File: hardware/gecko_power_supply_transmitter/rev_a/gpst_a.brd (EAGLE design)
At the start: 32.5 x 38.7 mm, 7 parts, among them J1 EPIC-PROG-POGO-NO-LEGS, J2 GECKO_POWER_SUPPLY_CONN, U1 EPIC-CORE_A

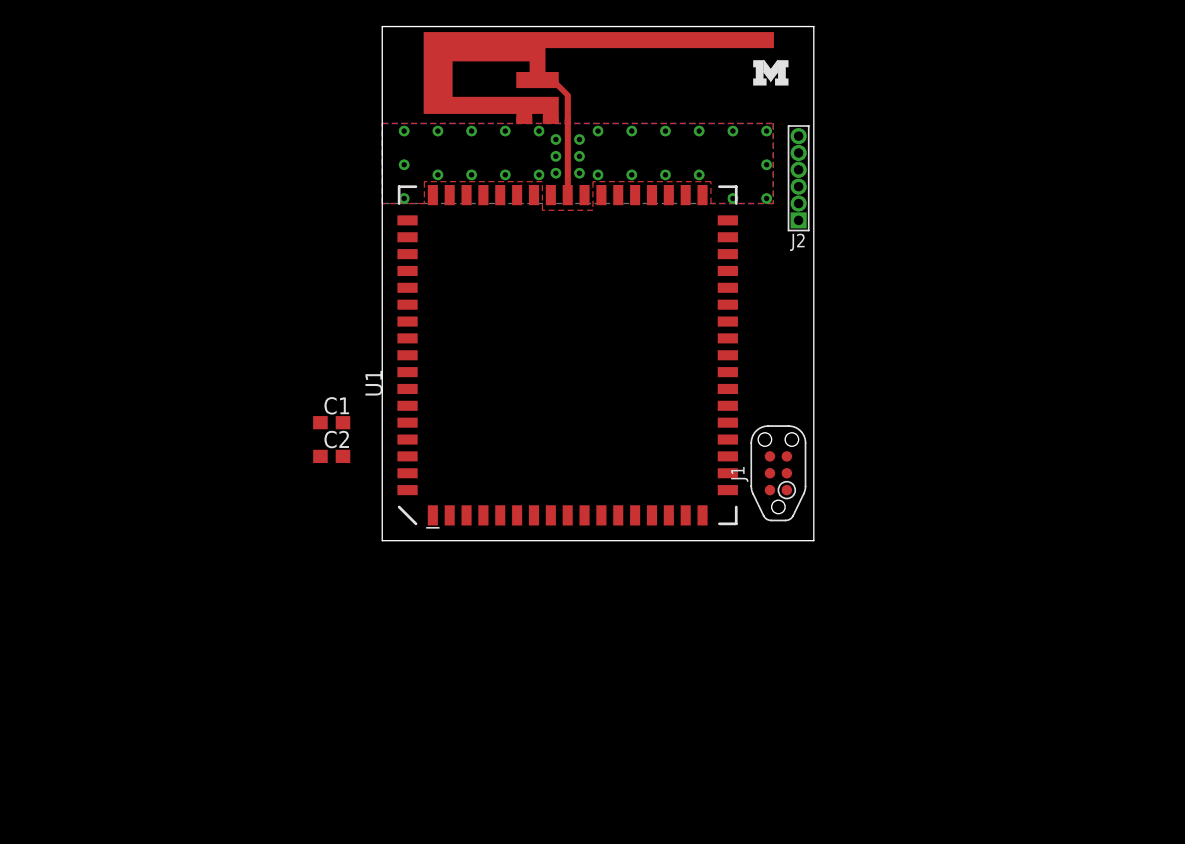
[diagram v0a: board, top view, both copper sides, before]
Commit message: no longer using epic
cc2538 and chip antenna ftw
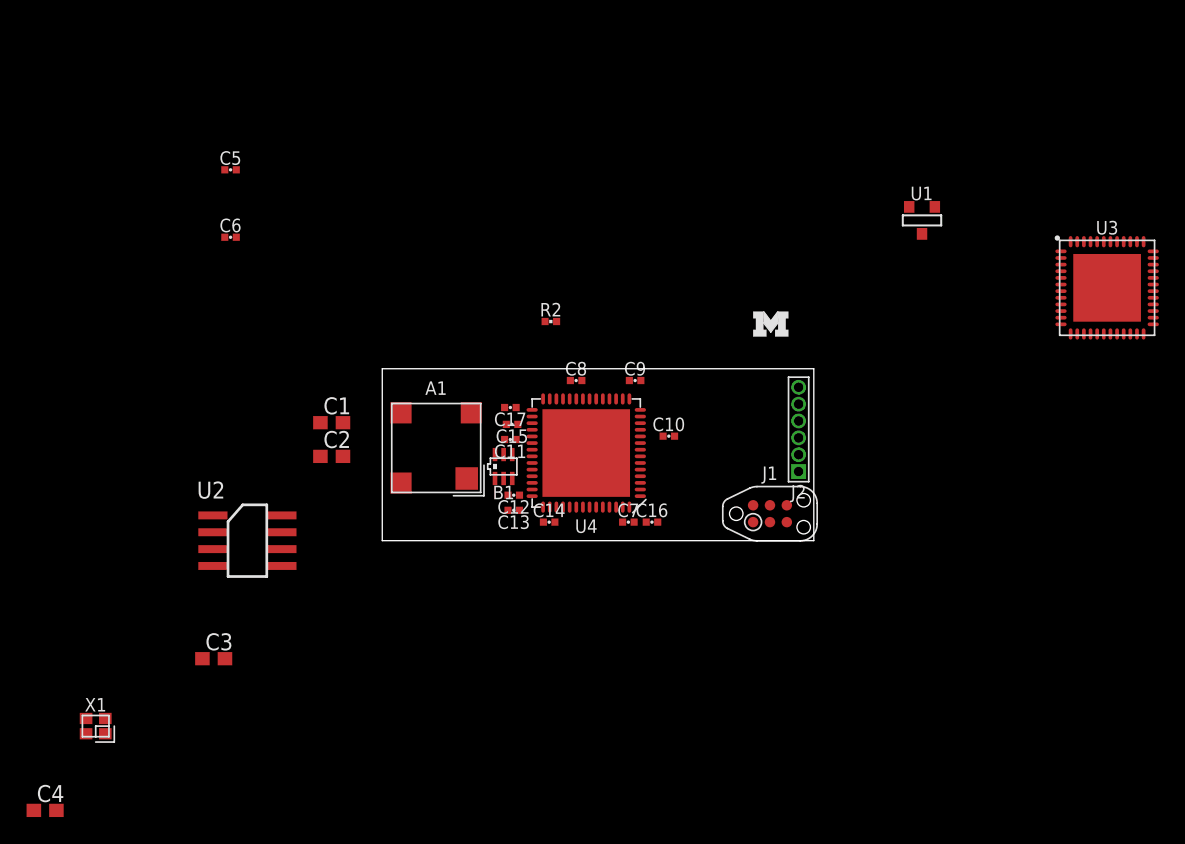
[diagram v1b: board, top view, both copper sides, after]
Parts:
- removed ANT1: PIFA-2.4GHZ, epic:PIFA-2.4GHZ
- added A1: FRACTUS-2.4GHZ-FR05-S1-N-0-001, chips:FRACTUS-ANTENNA-FR05-S1-N-0-001
- added B1: 2450BM15A0002, chips:2450BM
- added C10, C11, C12, C14, C15, C8, C9: 100nF, passives:0402_CAP
- added C13: 220pF, passives:0402_CAP
- added C16, C17, C7: 1uF, passives:0402_CAP
- added C3, C4: 0.1uF, rcl:C0603
- added C5, C6: 12pF, passives:0402_CAP
- added R2: (no value), passives:0402_RES
- added U2: FM25LB, chips:SOIC_8
- added U3: MSP430FR5969, chips:RGZ(S-PQFP-N48)
- added U4: CC2538, chips:S-PVQFN-N56
- added X1: EPSON-FA-128, crystals:FA-128
- U1: value EPIC-CORE_A -> DS2411; device epic:EPIC-LCC68 -> chips:SOT-23
- moved U1 28.5 mm to (40.6, 24.1), turned to 0 degrees
- moved J2 18.9 mm to (31.4, 7.75)
- moved U$1 18.9 mm to (27.9, 15.4)
- moved J1 3.11 mm to (29.2, 2.03), turned to 0 degrees
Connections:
- removed net N$1: ANT1.P$1, U1.P$43
- removed net RFGND: ANT1.P$2, ANT1.P$3, U1.P$42, U1.P$44
- new net N$10: C6.1, U4.35, X1.3
- new net N$15: C16.1, C17.1, U4.32, U4.56
- new net N$5: B1.4, U4.37
- new net N$6: B1.3, U4.38
- new net N$7: A1.1, B1.1
- new net N$9: C5.1, U4.34, X1.1
- net !RST: no longer U1.P$16
- net GND: now also B1.2, B1.5, B1.6, C10.2, C11.2, C12.2, C13.2, C14.2, C15.2, C16.2, C17.2, C3.2, C5.2, C6.2, C7.2, C8.2, C9.2, U2.P4, U4.VSS_QFN, X1.2, X1.4; no longer U1.P$1, U1.P$18, U1.P$35, U1.P$52
- net RX: no longer U1.P$62
- net TCK: no longer U1.P$15
- net TX: no longer U1.P$61
- net VCC: now also C10.1, C11.1, C12.1, C13.1, C14.1, C15.1, C3.1, C7.1, C8.1, C9.1, U2.P8, U4.10, U4.15, U4.24, U4.33, U4.36, U4.39, U4.40, U4.41, U4.43, U4.55; no longer U1.P$17, U1.P$68
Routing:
- net N$1: track 5.61 -> 0.00 mm
- removed copper zone on layer 1, net RFGND
- removed copper zone on layer 16, net RFGND
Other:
- board size 32.5 x 38.7 mm -> 32.5 x 13 mm

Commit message: routed except for vcc
the transmitter board is coming along nicely.
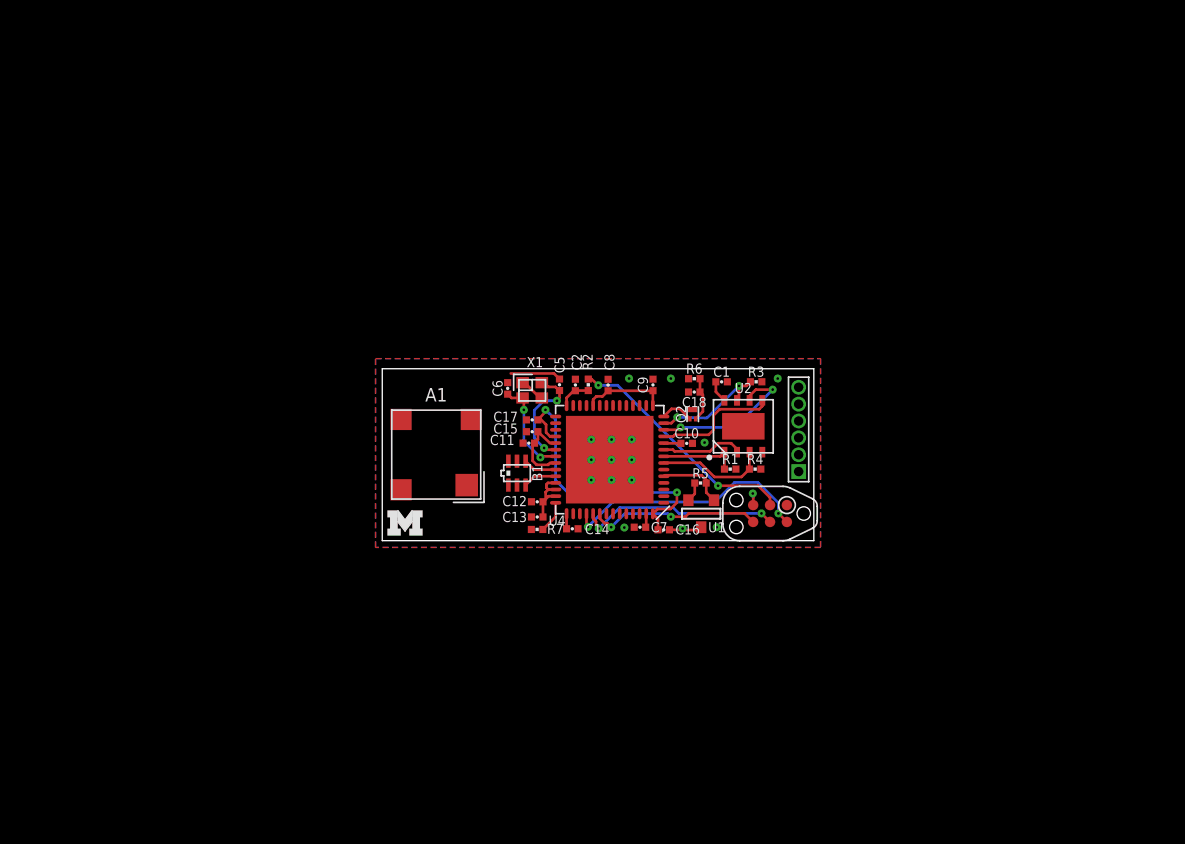
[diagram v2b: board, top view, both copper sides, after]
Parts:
- removed C3, C4: 0.1uF, rcl:C0603
- removed J1: EPIC-PROG-POGO-NO-LEGS, epic:TC2030-IDC-NL
- removed U3: MSP430FR5969, chips:RGZ(S-PQFP-N48)
- added C18: 2.2uF, passives:0402_CAP
- added J3: TC2030-CTX-NL, connector:TC2030-IDC-NL
- added Q2: MOSFET-NCHANNELXFDN-3, fets:XFDFN-3
- added R1, R3, R4: 4.7k, passives:0402_RES
- added R5: 2.2k, passives:0402_RES
- added R6: 4.7M, passives:0402_RES
- added R7: 56k, passives:0402_RES
- C1: device rcl:C0603 -> passives:0402_CAP
- C2: value 0.1uF -> 1nF; device rcl:C0603 -> passives:0402_CAP
- R2: value (none) -> 2.2k
- U2: value FM25LB -> FM25LBTDFN-8; device chips:SOIC_8 -> chips:TDFN-8
- moved X1 41.5 mm to (11.3, 11.3), turned to 180 degrees
- moved U2 38.3 mm to (27.2, 8.62)
- moved U$1 31.4 mm to (0.38, 0.38)
- moved C5 29.6 mm to (13.4, 11.7), turned to 90 degrees
- moved C1 29.5 mm to (25.6, 12.0)
- moved U1 27.7 mm to (24.0, 2.03)
- moved C6 23.8 mm to (9.45, 11.5), turned to 90 degrees
- moved C2 19.1 mm to (14.6, 11.7), turned to 90 degrees
- moved R2 5.54 mm to (15.5, 11.7), turned to 270 degrees
- moved C8 2.43 mm to (17.0, 11.7), turned to 90 degrees
- moved C17 1.89 mm to (11.3, 9.10)
- moved C12 1.84 mm to (11.7, 2.93)
- moved C13 1.84 mm to (11.7, 1.79)
- moved U4 1.84 mm to (17.1, 6.10)
- moved C14 1.81 mm to (14.3, 0.90)
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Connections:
- removed net !RST: J1.6
- removed net RX: J1.4
- removed net TX: J1.3
- new net !FRAM_CS: R1.1, U2.1, U4.8
- new net !FRAM_HOLD: R3.1, U2.7, U4.13
- new net !FRAM_WP: R4.1, U2.3, U4.7
- new net !RESET: J3.3, R2.1
- new net DS2411: R5.1, U1.1, U4.5
- new net MISO: U2.2, U4.9
- new net MOSI: U2.5, U4.11
- new net N$1: C2.1, R2.2, U4.28
- new net N$11: C18.1, Q2.S, R6.2
- new net SCK: U2.6, U4.12
- new net TDI: U4.49
- new net TDO: J3.6, U4.48
- new net TIME_CTL: Q2.G, U4.14
- new net TMS: J3.2, U4.46
- net GND: now also C18.2, C2.2, J3.5, R6.1, R7.2, U1.3, U2.4; no longer C3.2, J1.2, U2.P4
- net N$8: now also R7.1, U4.42; no longer C2.2
- net TCK: now also J3.4, U4.47; no longer J1.5
- net VCC: now also J3.1, Q2.D, R1.2, R3.2, R4.2, R5.2, U1.2, U2.8; no longer C2.1, C3.1, J1.1, U2.P8
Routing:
- net VCC: track 0.00 -> 24.0 mm
- net N$15: track 0.00 -> 22.7 mm, vias 0 -> 2
- net TMS: track 0.00 -> 19.1 mm, vias 0 -> 2
- net !RESET: track 0.00 -> 17.9 mm, vias 0 -> 2
- net TCK: track 0.00 -> 15.3 mm, vias 0 -> 2
- net TDO: track 0.00 -> 13.6 mm, vias 0 -> 2
- net SCK: track 0.00 -> 12.0 mm, vias 0 -> 2
- net MOSI: track 0.00 -> 9.43 mm
- net GND: track 0.00 -> 9.13 mm, vias 0 -> 17
- net !FRAM_HOLD: track 0.00 -> 8.99 mm, vias 0 -> 2
- net N$9: track 0.00 -> 8.45 mm, vias 0 -> 2
- net !FRAM_WP: track 0.00 -> 8.42 mm
- net N$10: track 0.00 -> 7.46 mm, vias 0 -> 2
- net MISO: track 0.00 -> 6.24 mm
- net !FRAM_CS: track 0.00 -> 5.97 mm
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- added copper zone on layer 1, net GND
- added copper zone on layer 16, net GND

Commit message: getting closer with vcc
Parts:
- moved B1 0.51 mm to (9.64, 5.09)
- moved C15 0.46 mm to (11.0, 8.59)
- moved C11 0.43 mm to (11.0, 7.78)
- moved C17 0.42 mm to (11.0, 9.43)
- moved C10 0.33 mm to (23.3, 7.33)
- moved R5 0.20 mm to (24.0, 4.14)
- moved R1 0.18 mm to (26.3, 5.57)
- moved C18 0.10 mm to (23.5, 11.3)
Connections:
- removed net N$11: C18.1, Q2.S, R6.2
- new net V_TIMER: C18.1, Q2.S, R6.2, U4.16
- net SHD: now also U4.6
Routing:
- net VCC: track 24.0 -> 62.7 mm, vias 0 -> 9
- net SHD: track 0.00 -> 12.2 mm, vias 0 -> 1
- net V_TIMER: track 0.00 -> 9.22 mm, vias 0 -> 2
- net GND: track 9.13 -> 13.1 mm, vias 17 -> 21
- net N$11: track 3.34 -> 0.00 mm
- net N$10: track 7.46 -> 8.72 mm
- net !RESET: track 17.9 -> 19.1 mm
- net N$6: track 2.54 -> 3.04 mm
- net N$5: track 2.52 -> 3.03 mm

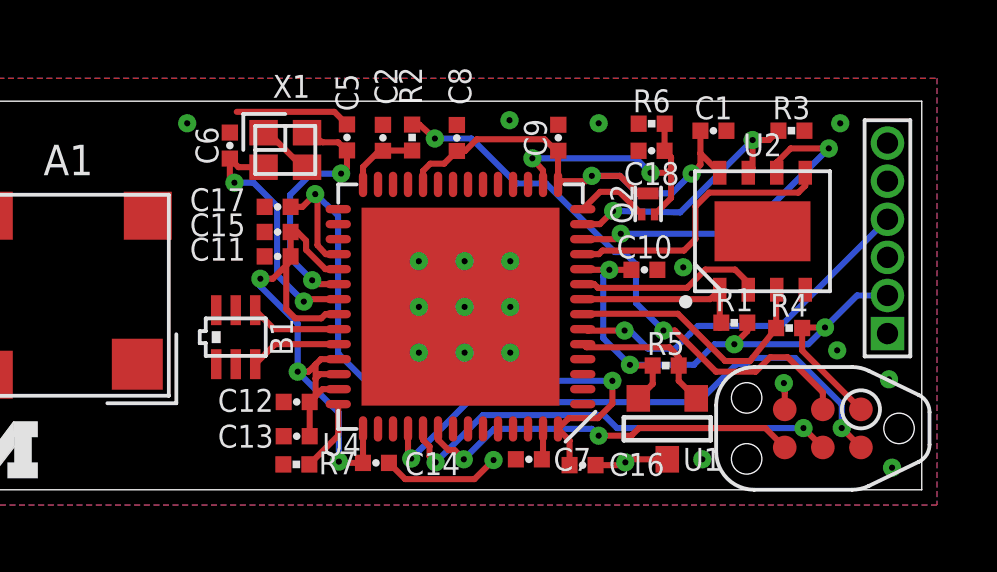
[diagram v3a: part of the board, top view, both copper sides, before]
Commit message: routed except antenna
now 4 layers cause its easier
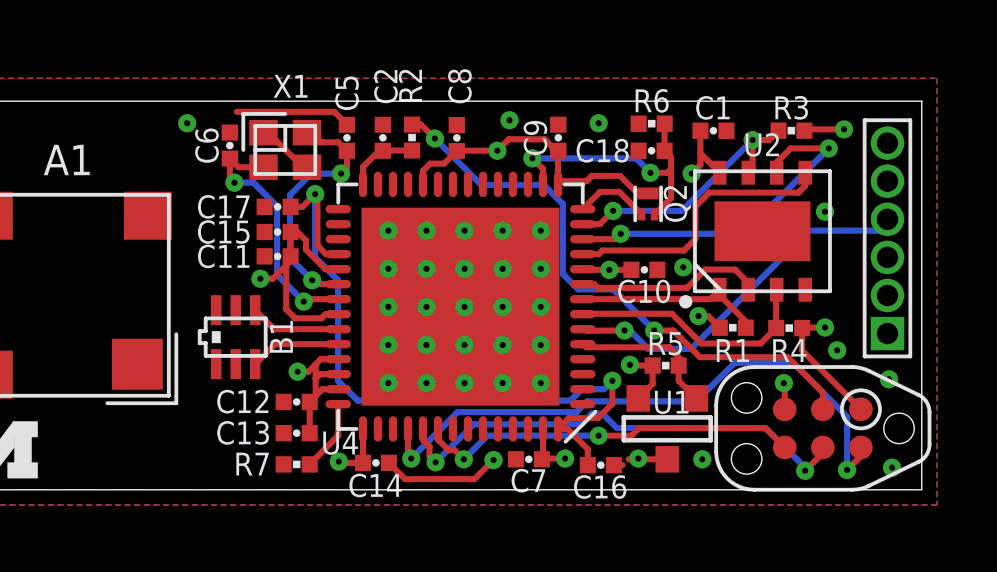
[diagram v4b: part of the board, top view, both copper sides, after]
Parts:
- moved C16 0.61 mm to (21.8, 0.82)
- moved R1 0.17 mm to (26.2, 5.40), turned to 180 degrees
- moved C13 0.10 mm to (11.7, 1.89)
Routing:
- net VCC: track 62.7 -> 40.5 mm, vias 9 -> 11
- net N$15: track 23.0 -> 24.5 mm
- net TMS: track 19.1 -> 20.3 mm
- net GND: track 13.1 -> 12.2 mm, vias 21 -> 37
- net TCK: track 15.3 -> 16.1 mm
- net !FRAM_WP: track 8.92 -> 8.36 mm
- added copper zone on layer 2, net GND
- added copper zone on layer 15, net VCC
